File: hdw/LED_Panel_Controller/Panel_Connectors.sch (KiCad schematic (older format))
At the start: 8 parts

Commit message: made a lot more schematic progress
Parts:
- gave numbers to parts that had none: 1
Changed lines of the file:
@@
 AR Path="/5BAAE10E/5CBDEB4C" Ref="ECO?"  Part="1"
 AR Path="/5BAAE2CE/5CBDEB4C" Ref="ECO?"  Part="1"
-AR Path="/5F583BFC/5CBDEB4C" Ref="C?"  Part="1"
-F 0 "C?" H 1675 3980 50  0000 L CNN
+AR Path="/5F583BFC/5CBDEB4C" Ref="ECO?"  Part="1"
+F 0 "ECO?" H 1675 3980 50  0000 L CNN
 F 1 "15pF" H 1675 3780 50  0000 L CNN
 F 2 "Capacitors_SMD:C_0603" H 1688 3730 50  0001 C CNN

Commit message: more schematic progress
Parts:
- C?: renamed from ECO?; Configuration (none) -> DNP
- J?: footprint Connectors_IDC:IDC-Header_2x08_Pitch2.54mm_Straight -> Connector_PinSocket_2.54mm:PinSocket_2x08_P2.54mm_Vertical
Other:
- note added: "Place on Bottom"
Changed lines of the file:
@@
 F 0 "J?" H 3300 4247 50  0000 C CNN
 F 1 "Panel Data" H 3300 4156 50  0000 C CNN
-F 2 "Connectors_IDC:IDC-Header_2x08_Pitch2.54mm_Straight" H 3250 3730 50  0001 C CNN
+F 2 "Connector_PinSocket_2.54mm:PinSocket_2x08_P2.54mm_Vertical" H 3250 3730 50  0001 C CNN
 F 3 "~" H 3250 3730 50  0001 C CNN
 F 4 "ED10523-ND" H 700 1930 50  0001 C CNN "Digi-Key PN"
@@
 AR Path="/5BAAE10E/5CBDEB4C" Ref="ECO?"  Part="1"
 AR Path="/5BAAE2CE/5CBDEB4C" Ref="ECO?"  Part="1"
-AR Path="/5F583BFC/5CBDEB4C" Ref="ECO?"  Part="1"
-F 0 "ECO?" H 1675 3980 50  0000 L CNN
+AR Path="/5F583BFC/5CBDEB4C" Ref="C?"  Part="1"
+F 0 "C?" H 1675 3980 50  0000 L CNN
 F 1 "15pF" H 1675 3780 50  0000 L CNN
 F 2 "Capacitors_SMD:C_0603" H 1688 3730 50  0001 C CNN
@@
 F 6 "50V" H 1500 3880 50  0000 R CNN "Voltage"
 F 7 "NP0" H 1500 3780 50  0000 R CNN "Dielectric"
+F 8 "DNP" H 1870 3880 50  0000 C CNN "Configuration"
 	1    1650 3880
 	1    0    0    -1
@@
 	2780 5830 2780 5750
 Connection ~ 2780 5750
+Text Notes 3010 4480 0    50   ~ 0
+Place on Bottom
 $EndSCHEMATC

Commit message: more schematic development
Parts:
- gave numbers to parts that had none: 1
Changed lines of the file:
@@
 $Descr A 11000 8500
 encoding utf-8
-Sheet 32 34
+Sheet 33 34
 Title "LED Panel Controller"
-Date "2020-12-23"
+Date "2021-03-24"
 Rev "A"
-Comp "Drew Maatman, Logan Wedel"
+Comp "Drew Maatman"
 Comment1 ""
 Comment2 ""
@@
 AR Path="/5BAAE10E/5CBDEB4C" Ref="ECO?"  Part="1"
 AR Path="/5BAAE2CE/5CBDEB4C" Ref="ECO?"  Part="1"
-AR Path="/5F583BFC/5CBDEB4C" Ref="C?"  Part="1"
-F 0 "C?" H 1675 3980 50  0000 L CNN
+AR Path="/5F583BFC/5CBDEB4C" Ref="ECO?"  Part="1"
+F 0 "ECO?" H 1675 3980 50  0000 L CNN
 F 1 "15pF" H 1675 3780 50  0000 L CNN
 F 2 "Capacitors_SMD:C_0603" H 1688 3730 50  0001 C CNN

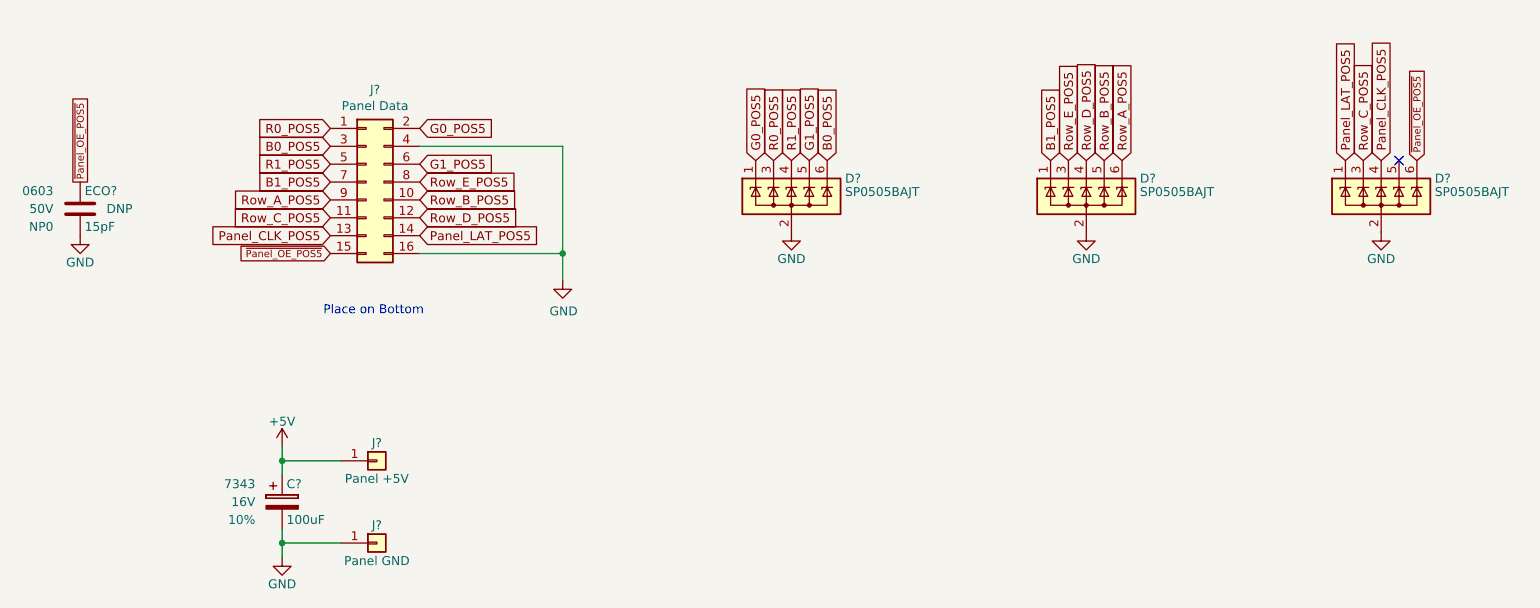
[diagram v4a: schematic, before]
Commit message: added digikey pns, footprints, bom scrubbed
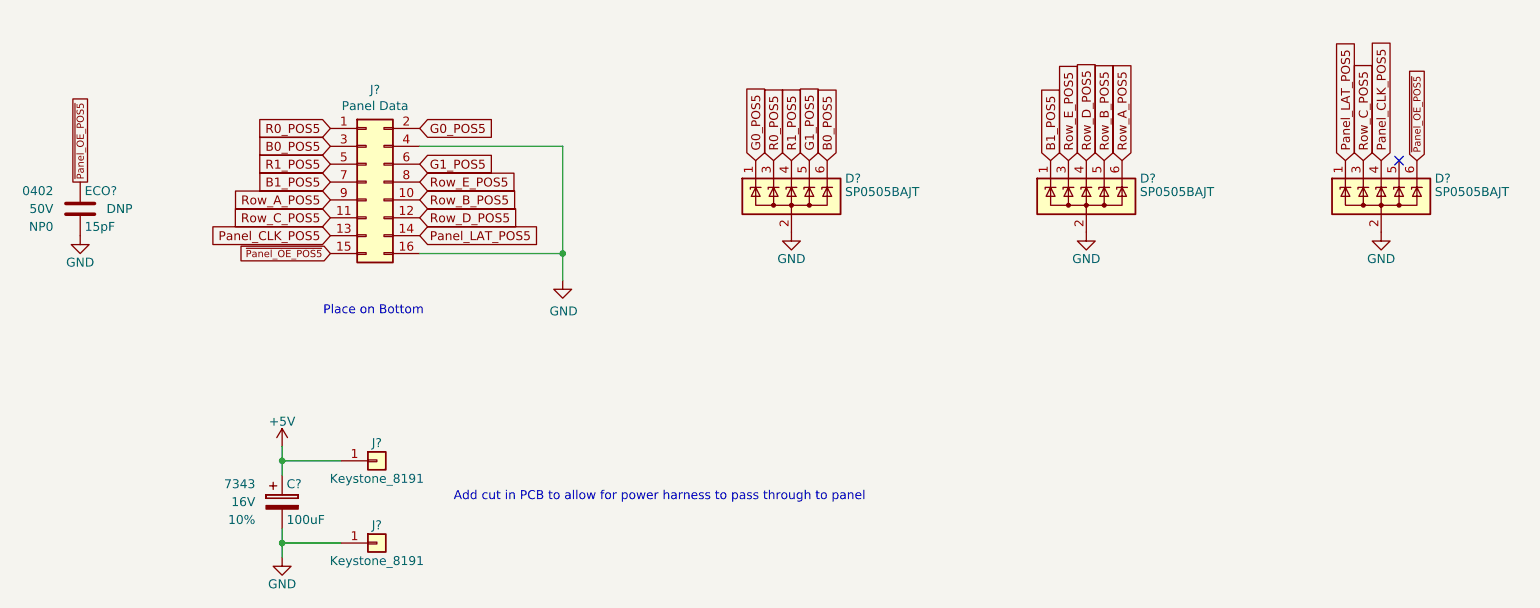
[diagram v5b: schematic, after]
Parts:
- C?: renamed from ECO?; footprint Capacitors_SMD:C_0603 -> Capacitors_SMD:C_0402; Digi-Key PN 478-10289-1-ND -> 587-1949-1-ND; display_footprint 0603 -> 0402
- J?: Digi-Key PN ED10523-ND -> S9196-ND
- J?: value Panel +5V -> Keystone_8191; footprint Custom Footprints Library:Wuerth_7461096_M4_Shank_9pos -> Custom Footprints Library:Keystone_8191; Digi-Key PN (none) -> 36-8191-ND
- J?: value Panel GND -> Keystone_8191; footprint Custom Footprints Library:Wuerth_7461096_M4_Shank_9pos -> Custom Footprints Library:Keystone_8191; Digi-Key PN (none) -> 36-8191-ND
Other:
- note added: "Add cut in PCB to allow for power harness to pass through to panel"
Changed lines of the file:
@@
 F 2 "Connector_PinSocket_2.54mm:PinSocket_2x08_P2.54mm_Vertical" H 3250 3730 50  0001 C CNN
 F 3 "~" H 3250 3730 50  0001 C CNN
-F 4 "ED10523-ND" H 700 1930 50  0001 C CNN "Digi-Key PN"
+F 4 "S9196-ND" H 700 1930 50  0001 C CNN "Digi-Key PN"
 	1    3250 3730
 	1    0    0    -1
@@
 AR Path="/5BAAE10E/5CBDEB4C" Ref="ECO?"  Part="1"
 AR Path="/5BAAE2CE/5CBDEB4C" Ref="ECO?"  Part="1"
-AR Path="/5F583BFC/5CBDEB4C" Ref="ECO?"  Part="1"
-F 0 "ECO?" H 1675 3980 50  0000 L CNN
+AR Path="/5F583BFC/5CBDEB4C" Ref="C?"  Part="1"
+F 0 "C?" H 1675 3980 50  0000 L CNN
 F 1 "15pF" H 1675 3780 50  0000 L CNN
-F 2 "Capacitors_SMD:C_0603" H 1688 3730 50  0001 C CNN
+F 2 "Capacitors_SMD:C_0402" H 1688 3730 50  0001 C CNN
 F 3 "" H 1675 3980 50  0001 C CNN
-F 4 "478-10289-1-ND" H 1650 3880 50  0001 C CNN "Digi-Key PN"
-F 5 "0603" H 1500 3980 50  0000 R CNN "display_footprint"
+F 4 "587-1949-1-ND" H 1650 3880 50  0001 C CNN "Digi-Key PN"
+F 5 "0402" H 1500 3980 50  0000 R CNN "display_footprint"
 F 6 "50V" H 1500 3880 50  0000 R CNN "Voltage"
 F 7 "NP0" H 1500 3780 50  0000 R CNN "Dielectric"
@@
 P 3310 5290
 F 0 "J?" H 3310 5390 50  0000 C CNN
-F 1 "Panel +5V" H 3310 5190 50  0000 C CNN
-F 2 "Custom Footprints Library:Wuerth_7461096_M4_Shank_9pos" H 3310 5290 50  0001 C CNN
+F 1 "Keystone_8191" H 3310 5190 50  0000 C CNN
+F 2 "Custom Footprints Library:Keystone_8191" H 3310 5290 50  0001 C CNN
 F 3 "~" H 3310 5290 50  0001 C CNN
+F 4 "36-8191-ND" H 3310 5290 50  0001 C CNN "Digi-Key PN"
 	1    3310 5290
 	1    0    0    -1
@@
 P 3310 5750
 F 0 "J?" H 3310 5850 50  0000 C CNN
-F 1 "Panel GND" H 3310 5650 50  0000 C CNN
-F 2 "Custom Footprints Library:Wuerth_7461096_M4_Shank_9pos" H 3310 5750 50  0001 C CNN
+F 1 "Keystone_8191" H 3310 5650 50  0000 C CNN
+F 2 "Custom Footprints Library:Keystone_8191" H 3310 5750 50  0001 C CNN
 F 3 "~" H 3310 5750 50  0001 C CNN
+F 4 "36-8191-ND" H 3310 5750 50  0001 C CNN "Digi-Key PN"
 	1    3310 5750
 	1    0    0    -1
@@
 Text Notes 3010 4480 0    50   ~ 0
 Place on Bottom
+Text Notes 3740 5520 0    50   ~ 0
+Add cut in PCB to allow for power harness to pass through to panel
 $EndSCHEMATC

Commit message: assigned I2C addresses
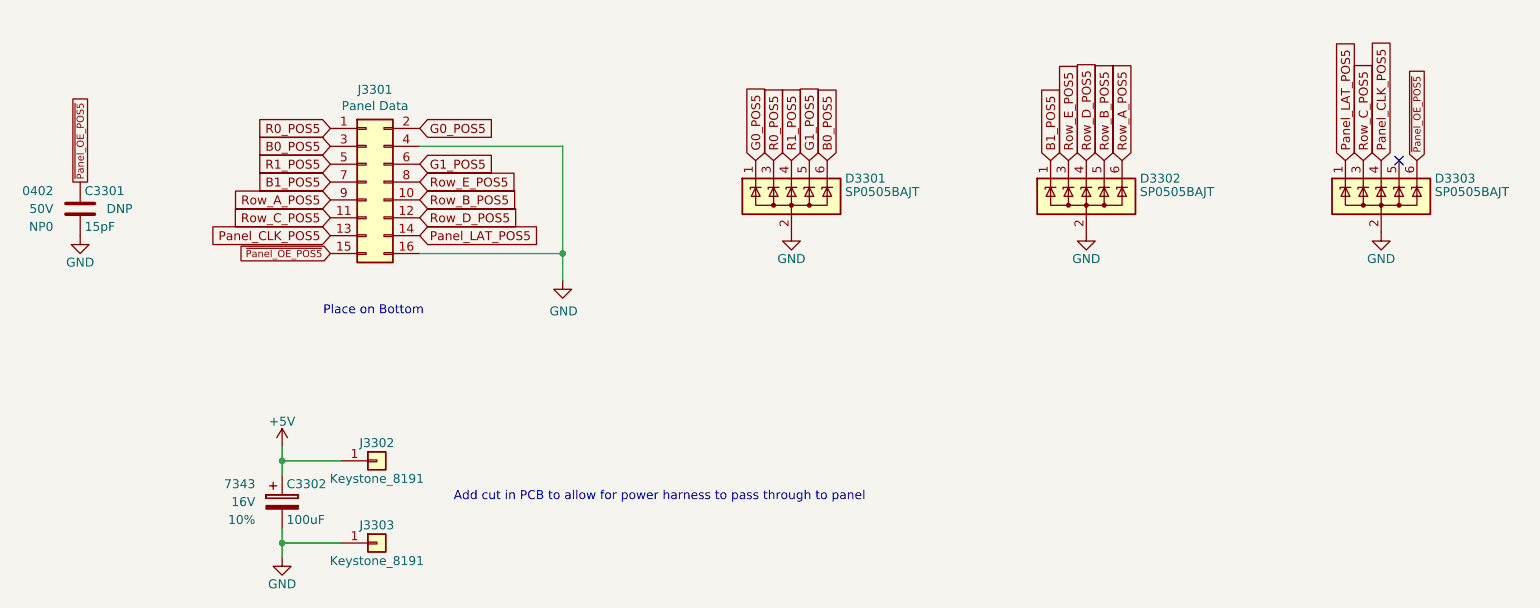
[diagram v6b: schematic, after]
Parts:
- gave numbers to parts that had none: 8
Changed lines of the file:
@@
 $EndDescr
 $Comp
-L Connector_Generic:Conn_02x08_Odd_Even J?
+L Connector_Generic:Conn_02x08_Odd_Even J3301
 U 1 1 5BB405EB
 P 3250 3730
-F 0 "J?" H 3300 4247 50  0000 C CNN
+F 0 "J3301" H 3300 4247 50  0000 C CNN
 F 1 "Panel Data" H 3300 4156 50  0000 C CNN
 F 2 "Connector_PinSocket_2.54mm:PinSocket_2x08_P2.54mm_Vertical" H 3250 3730 50  0001 C CNN
@@
 G1_POS5
 $Comp
-L power:GND #PWR?
+L power:GND #PWR03304
 U 1 1 5BB40845
 P 4350 4280
-F 0 "#PWR?" H 4350 4030 50  0001 C CNN
+F 0 "#PWR03304" H 4350 4030 50  0001 C CNN
 F 1 "GND" H 4355 4107 50  0000 C CNN
 F 2 "" H 4350 4280 50  0001 C CNN
@@
 G1_POS5
 $Comp
-L Power_Protection:SP0505BAJT D?
+L Power_Protection:SP0505BAJT D3301
 U 1 1 5C14E3A9
 P 5630 3810
-F 0 "D?" H 5930 3910 50  0000 L CNN
+F 0 "D3301" H 5930 3910 50  0000 L CNN
 F 1 "SP0505BAJT" H 5930 3835 50  0000 L CNN
 F 2 "TO_SOT_Packages_SMD:SOT-363_SC-70-6" H 5930 3760 50  0001 L CNN
@@
 $EndComp
 $Comp
-L power:GND #PWR?
+L power:GND #PWR03305
 U 1 1 5C150614
 P 5630 4010
-F 0 "#PWR?" H 5630 3760 50  0001 C CNN
+F 0 "#PWR03305" H 5630 3760 50  0001 C CNN
 F 1 "GND" H 5630 3860 50  0000 C CNN
 F 2 "" H 5630 4010 50  0001 C CNN
@@
 $EndComp
 $Comp
-L Power_Protection:SP0505BAJT D?
+L Power_Protection:SP0505BAJT D3302
 U 1 1 5C150760
 P 7280 3810
-F 0 "D?" H 7580 3910 50  0000 L CNN
+F 0 "D3302" H 7580 3910 50  0000 L CNN
 F 1 "SP0505BAJT" H 7580 3835 50  0000 L CNN
 F 2 "TO_SOT_Packages_SMD:SOT-363_SC-70-6" H 7580 3760 50  0001 L CNN
@@
 $EndComp
 $Comp
-L power:GND #PWR?
+L power:GND #PWR03306
 U 1 1 5C150767
 P 7280 4010
-F 0 "#PWR?" H 7280 3760 50  0001 C CNN
+F 0 "#PWR03306" H 7280 3760 50  0001 C CNN
 F 1 "GND" H 7280 3860 50  0000 C CNN
 F 2 "" H 7280 4010 50  0001 C CNN
@@
 $EndComp
 $Comp
-L Power_Protection:SP0505BAJT D?
+L Power_Protection:SP0505BAJT D3303
 U 1 1 5C150847
 P 8930 3810
-F 0 "D?" H 9230 3910 50  0000 L CNN
+F 0 "D3303" H 9230 3910 50  0000 L CNN
 F 1 "SP0505BAJT" H 9230 3835 50  0000 L CNN
 F 2 "TO_SOT_Packages_SMD:SOT-363_SC-70-6" H 9230 3760 50  0001 L CNN
@@
 $EndComp
 $Comp
-L power:GND #PWR?
+L power:GND #PWR03307
 U 1 1 5C15084E
 P 8930 4010
-F 0 "#PWR?" H 8930 3760 50  0001 C CNN
+F 0 "#PWR03307" H 8930 3760 50  0001 C CNN
 F 1 "GND" H 8930 3860 50  0000 C CNN
 F 2 "" H 8930 4010 50  0001 C CNN
@@
 AR Path="/5BAAE10E/5CBDEB4C" Ref="ECO?"  Part="1"
 AR Path="/5BAAE2CE/5CBDEB4C" Ref="ECO?"  Part="1"
-AR Path="/5F583BFC/5CBDEB4C" Ref="C?"  Part="1"
-F 0 "C?" H 1675 3980 50  0000 L CNN
+AR Path="/5F583BFC/5CBDEB4C" Ref="C3301"  Part="1"
+F 0 "C3301" H 1675 3980 50  0000 L CNN
 F 1 "15pF" H 1675 3780 50  0000 L CNN
 F 2 "Capacitors_SMD:C_0402" H 1688 3730 50  0001 C CNN
@@
 ~Panel_OE_POS5
 $Comp
-L power:GND #PWR?
+L power:GND #PWR03301
 U 1 1 5CBDEF57
 P 1650 4030
-F 0 "#PWR?" H 1650 3780 50  0001 C CNN
+F 0 "#PWR03301" H 1650 3780 50  0001 C CNN
 F 1 "GND" H 1650 3880 50  0000 C CNN
 F 2 "" H 1650 4030 50  0001 C CNN
@@
 $EndComp
 $Comp
-L Connector_Generic:Conn_01x01 J?
+L Connector_Generic:Conn_01x01 J3302
 U 1 1 5F739EFA
 P 3310 5290
-F 0 "J?" H 3310 5390 50  0000 C CNN
+F 0 "J3302" H 3310 5390 50  0000 C CNN
 F 1 "Keystone_8191" H 3310 5190 50  0000 C CNN
 F 2 "Custom Footprints Library:Keystone_8191" H 3310 5290 50  0001 C CNN
@@
 $EndComp
 $Comp
-L Custom_Library:CP_Tant_Custom C?
+L Custom_Library:CP_Tant_Custom C3302
 U 1 1 5F73C920
 P 2780 5520
-F 0 "C?" H 2805 5620 50  0000 L CNN
+F 0 "C3302" H 2805 5620 50  0000 L CNN
 F 1 "100uF" H 2805 5420 50  0000 L CNN
 F 2 "Capacitors_Tantalum_SMD:CP_Tantalum_Case-X_EIA-7343-43_Reflow" H 2818 5370 50  0001 C CNN
@@
 	2780 5290 2780 5370
 $Comp
-L power:+5V #PWR?
+L power:+5V #PWR03302
 U 1 1 5F73CC26
 P 2780 5210
-F 0 "#PWR?" H 2780 5060 50  0001 C CNN
+F 0 "#PWR03302" H 2780 5060 50  0001 C CNN
 F 1 "+5V" H 2780 5350 50  0000 C CNN
 F 2 "" H 2780 5210 50  0001 C CNN
@@
 Connection ~ 2780 5290
 $Comp
-L Connector_Generic:Conn_01x01 J?
+L Connector_Generic:Conn_01x01 J3303
 U 1 1 5F73D389
 P 3310 5750
-F 0 "J?" H 3310 5850 50  0000 C CNN
+F 0 "J3303" H 3310 5850 50  0000 C CNN
 F 1 "Keystone_8191" H 3310 5650 50  0000 C CNN
 F 2 "Custom Footprints Library:Keystone_8191" H 3310 5750 50  0001 C CNN
@@
 	2780 5750 2780 5670
 $Comp
-L power:GND #PWR?
+L power:GND #PWR03303
 U 1 1 5F73DE40
 P 2780 5830
-F 0 "#PWR?" H 2780 5580 50  0001 C CNN
+F 0 "#PWR03303" H 2780 5580 50  0001 C CNN
 F 1 "GND" H 2780 5680 50  0000 C CNN
 F 2 "" H 2780 5830 50  0001 C CNN
